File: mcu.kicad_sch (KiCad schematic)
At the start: 9 parts, among them J25 SD_Card_Device, J26 SD_Card_Device

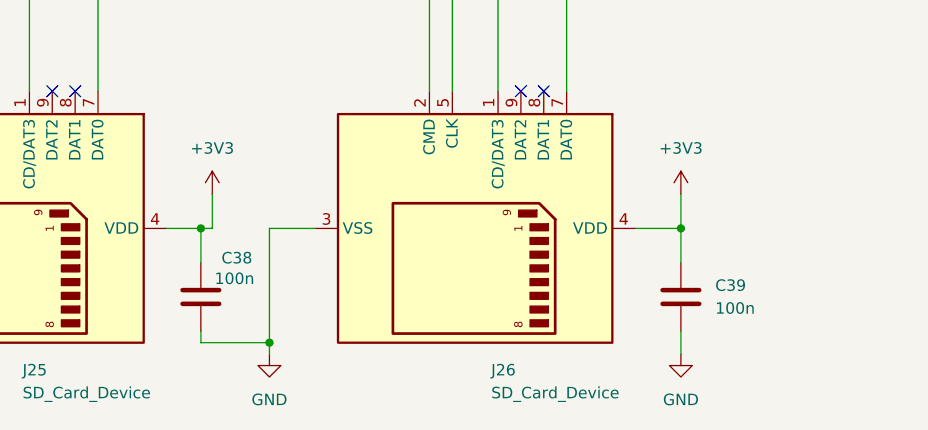
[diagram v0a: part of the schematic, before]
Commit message: Added SD card readers and USB-C for power in.
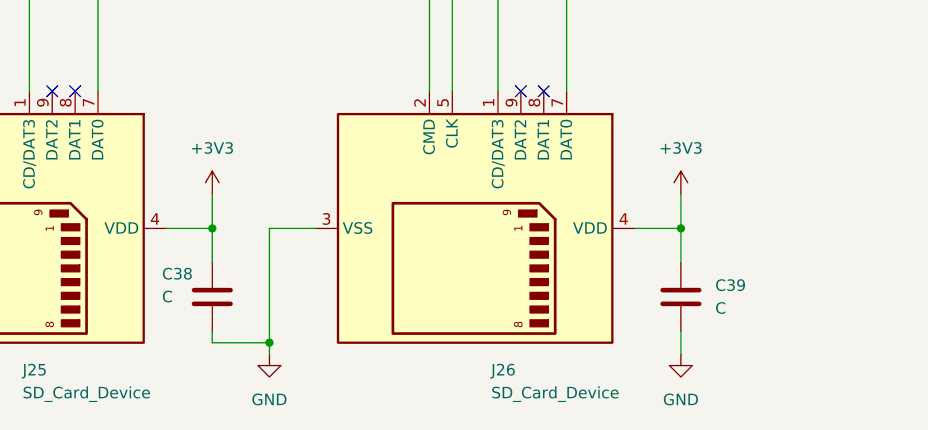
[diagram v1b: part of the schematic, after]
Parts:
- C38, C39: value 100n -> C
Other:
- moved on the sheet: C38
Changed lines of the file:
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@@
-	)
-	(junction
-		(at 72.39 157.48)
-		(diameter 0)
-		(color 0 0 0 0)
 	)
 	(junction
@@
 		(color 0 0 0 0)
 	)
+	(junction
+		(at 73.66 157.48)
+		(diameter 0)
+		(color 0 0 0 0)
+	)
 	(no_connect
 		(at 110.49 142.24)
@@
 	(wire
 		(pts
-			(xy 72.39 170.18) (xy 72.39 168.91)
+			(xy 73.66 170.18) (xy 73.66 168.91)
 		)
 		(stroke
@@
 	(wire
 		(pts
-			(xy 72.39 157.48) (xy 72.39 161.29)
+			(xy 73.66 157.48) (xy 73.66 161.29)
 		)
 		(stroke
@@
 	(wire
 		(pts
-			(xy 72.39 157.48) (xy 73.66 157.48)
-		)
-		(stroke
-			(width 0)
-			(type default)
-		)
-	)
-	(wire
-		(pts
 			(xy 167.64 82.55) (xy 226.06 82.55)
 		)
@@
 	(wire
 		(pts
+			(xy 73.66 157.48) (xy 68.58 157.48)
+		)
+		(stroke
+			(width 0)
+			(type default)
+		)
+	)
+	(wire
+		(pts
 			(xy 128.27 26.67) (xy 123.19 26.67)
 		)
@@
 	(wire
 		(pts
-			(xy 72.39 170.18) (xy 80.01 170.18)
+			(xy 73.66 170.18) (xy 80.01 170.18)
 		)
 		(stroke
@@
 		(pts
 			(xy 45.72 142.24) (xy 45.72 80.01)
-		)
-		(stroke
-			(width 0)
-			(type default)
-		)
-	)
-	(wire
-		(pts
-			(xy 72.39 157.48) (xy 68.58 157.48)
 		)
 		(stroke
@@
 	(symbol
 		(lib_id "Device:C")
-		(at 72.39 165.1 0)
+		(at 73.66 165.1 0)
 		(unit 1)
 		(exclude_from_sim no)
@@
 		(dnp no)
 		(property "Reference" "C38"
-			(at 74.676 160.782 0)
+			(at 68.072 162.56 0)
 			(effects
 				(font
@@
 			)
 		)
-		(property "Value" "100n"
-			(at 73.914 163.068 0)
+		(property "Value" "C"
+			(at 68.072 165.1 0)
 			(effects
 				(font
@@
 		)
 		(property "Footprint" ""
-			(at 73.3552 168.91 0)
+			(at 74.6252 168.91 0)
 			(effects
 				(font
@@
 		)
 		(property "Datasheet" "~"
-			(at 72.39 165.1 0)
+			(at 73.66 165.1 0)
 			(effects
 				(font
@@
 		)
 		(property "Description" "Unpolarized capacitor"
-			(at 72.39 165.1 0)
+			(at 73.66 165.1 0)
 			(effects
 				(font
@@
 			)
 		)
-		(property "Value" "100n"
+		(property "Value" "C"
 			(at 129.54 166.3699 0)
 			(effects

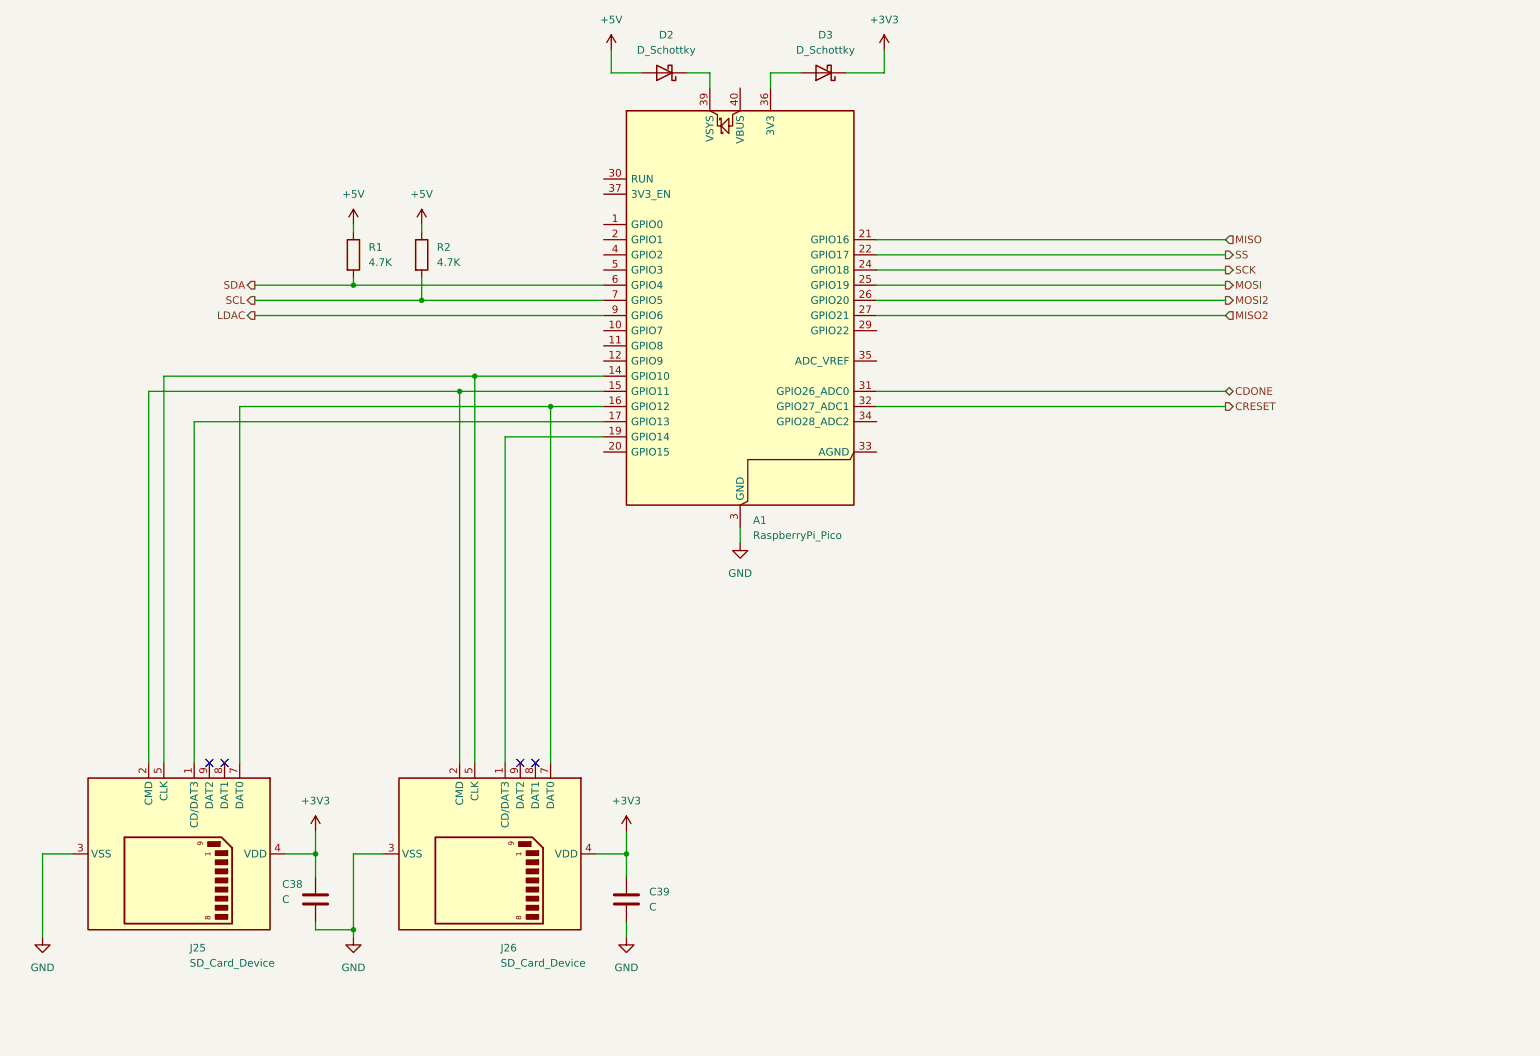
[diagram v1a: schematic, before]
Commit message: reroute dac + comparators
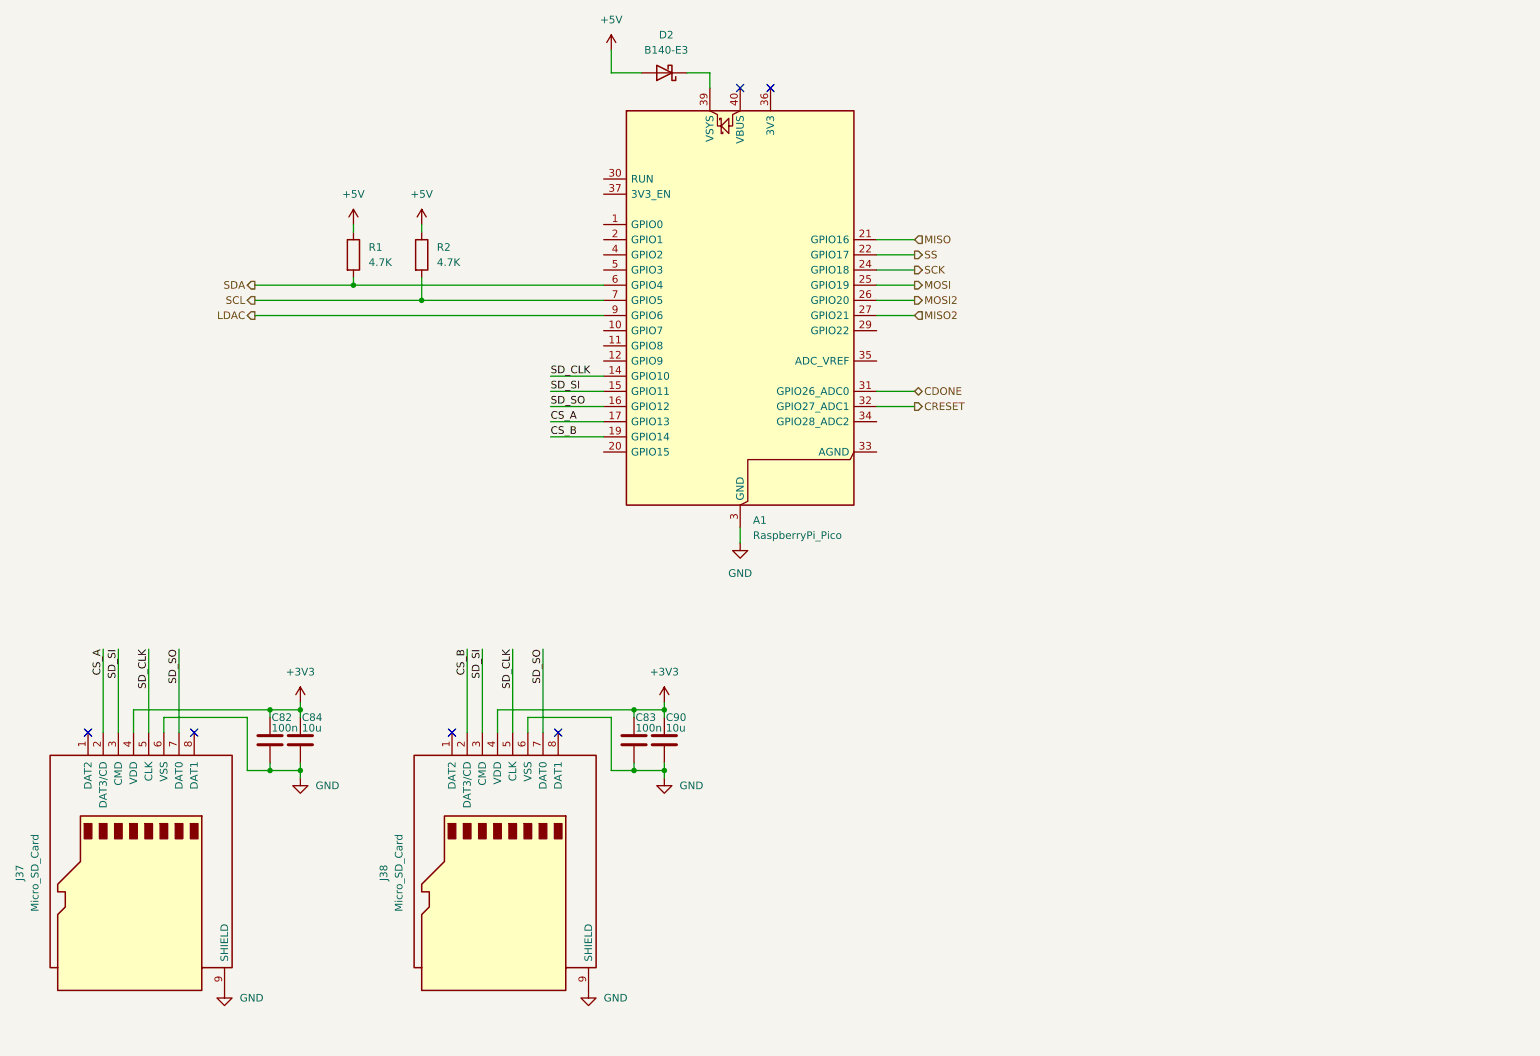
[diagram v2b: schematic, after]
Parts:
- removed C38, C39: C, symbol Device:C
- removed D3: D_Schottky, symbol Device:D_Schottky
- removed J25, J26: SD_Card_Device, symbol Connector:SD_Card_Device
- added C82, C83: 100n, symbol Device:C
- added C84, C90: 10u, symbol Device:C
- added J37, J38: Micro_SD_Card, symbol Connector:Micro_SD_Card
- D2: value D_Schottky -> B140-E3
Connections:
- net +3V3: now also C82.1, C83.1, C84.1, C90.1, J37.4 (VDD), J38.4 (VDD)
- net GND: now also C82.2, C83.2, C84.2, C90.2, J37.6 (VSS), J37.9 (SHIELD), J38.6 (VSS), J38.9 (SHIELD)
- net CS_B: now reaches A1.19 (GPIO14)
- net CS_B: now also J38.2 (DAT3/CD)
- net SD_SI: now reaches A1.15 (GPIO11)
- net SD_SI: now also J37.3 (CMD), J38.3 (CMD)
- net SD_CLK: now reaches A1.14 (GPIO10)
- net SD_CLK: now also J37.5 (CLK), J38.5 (CLK)
- net SD_SO: now reaches A1.16 (GPIO12)
- net SD_SO: now also J37.7 (DAT0), J38.7 (DAT0)
- net CS_A: now reaches A1.17 (GPIO13)
- net CS_A: now also J37.2 (DAT3/CD)
- no-connect marks 4 -> 6

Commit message: rewire
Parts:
- removed A1: RaspberryPi_Pico, Module:RaspberryPi_Pico_Common_Unspecified, symbol MCU_Module:RaspberryPi_Pico
- removed C83: 100n, symbol Device:C
- removed C84, C90: 10u, symbol Device:C
- removed D2: B140-E3, symbol Device:D_Schottky
- added C1, C3: 100n, symbol Device:C
- added C2, C4: 10u, symbol Device:C
- added C30, C31, C33, C35, C36, C5, C6, C7: 100n, Capacitor_SMD:C_0402_1005Metric, symbol Device:C
- added C32, C34: 1u 25V, Capacitor_SMD:C_0402_1005Metric, symbol Device:C
- added C8, C9: 15p, Capacitor_SMD:C_0402_1005Metric, symbol Device:C
- added JP4: ~{RESET}, Jumper:SolderJumper-2_P1.3mm_Open_RoundedPad1.0x1.5mm, symbol Jumper:SolderJumper_2_Open
- added JP5: ~{USB_BOOT}, Jumper:SolderJumper-2_P1.3mm_Open_RoundedPad1.0x1.5mm, symbol Jumper:SolderJumper_2_Open
- added R100, R101: 27R, Resistor_SMD:R_0402_1005Metric, symbol Device:R
- added R112: 10k, Resistor_SMD:R_0402_1005Metric, symbol Device:R
- added R113, R98, R99: 1k, Resistor_SMD:R_0402_1005Metric, symbol Device:R
- added R96, R97: 10k, symbol Device:R
- added U4: W25Q32JVZP, Package_SON:WSON-8-1EP_6x5mm_P1.27mm_EP3.4x4.3mm, symbol Memory_Flash:W25Q32JVZP
- added U5: RP2040, Package_DFN_QFN:QFN-56-1EP_7x7mm_P0.4mm_EP3.2x3.2mm, symbol MCU_RaspberryPi:RP2040
- added Y1: 12 MHz ABM8-272-T3, Crystal:Crystal_SMD_Abracon_ABM8AIG-4Pin_3.2x2.5mm, symbol Device:Crystal_GND24_Small
- C82: footprint (none) -> Capacitor_SMD:C_0402_1005Metric; LCSC (none) -> C307331
- R1, R2: value 4.7K -> 4.7k
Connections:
- net +5V is gone; now on net +3V3: R1.1, R2.1
- net +3V3: now also C33.1, C34.1, C35.1, C36.1, C5.1, C6.1, C7.1, R112.1, R96.1, R97.1, R98.2, U4.8 (VCC), U5.1 (IOVDD), U5.10 (IOVDD), U5.22 (IOVDD), U5.33 (IOVDD), U5.42 (IOVDD), U5.43 (ADC_AVDD), U5.44 (VREG_IN), U5.48 (USB_VDD), U5.49 (IOVDD); no longer J37.4 (VDD), J38.4 (VDD)
- net CS_A: now also U5.11 (GPIO8)
- net CS_B: now also U5.12 (GPIO9)
- net GND: now also C1.2, C2.2, C3.2, C30.2, C31.2, C32.2, C33.2, C34.2, C35.2, C36.2, C4.2, C5.2, C6.2, C7.2, C8.1, C9.1, JP4.1 (A), JP5.1 (A), U4.4 (GND), U4.9 (EP), U5.19 (TESTEN), U5.57 (GND), Y1.2, Y1.4
- net SD_CLK: now also U5.13 (GPIO10)
- net SD_SI: now also U5.14 (GPIO11)
- net SD_SO: now also U5.15 (GPIO12)
- net SCL renamed VREF_SCL
- net VREF_SCL: now also U5.3 (GPIO1)
- net SDA renamed VREF_SDA
- net VREF_SDA: now also U5.2 (GPIO0)
- new net: JP4.2 (B), R98.1, U5.26 (RUN)
- new net: JP5.2 (B), R99.1
- new net: R101.2, U5.46 (USB_DM)
- new net: R100.2, U5.47 (USB_DP)
- new net: C9.2, R113.1, Y1.3
- new net: C3.1, C4.1, J38.4 (VDD)
- new net: C1.1, C2.1, J37.4 (VDD)
- new net +1V1: C30.1, C31.1, C32.1, U5.23 (DVDD), U5.45 (VREG_VOUT), U5.50 (DVDD)
- new net FPGA_CDONE: R97.2, U5.17 (GPIO14)
- new net FPGA_~{CRESET}: R96.2, U5.16 (GPIO13)
- new net QSPI_SCLK: U4.6 (CLK), U5.52 (QSPI_SCLK)
- new net QSPI_SD0: U4.5 (DI/IO_{0}), U5.53 (QSPI_SD0)
- new net QSPI_SD1: U4.2 (DO/IO_{1}), U5.55 (QSPI_SD1)
- new net QSPI_SD2: U4.3 (~{WP}/IO_{2}), U5.54 (QSPI_SD2)
- new net QSPI_SD3: U4.7 (~{HOLD}/~{RESET}/IO_{3}), U5.51 (QSPI_SD3)
- new net QSPI_SS: R112.2, R99.2, U4.1 (~{CS}), U5.56 (QSPI_SS)
- new net SWCLK: U5.24 (SWCLK)
- new net SWD: U5.25 (SWD)
- new net USB_D+: R100.1
- new net USB_D-: R101.1
- new net XIN: C8.2, U5.20 (XIN), Y1.1
- new net XOUT: R113.2, U5.21 (XOUT)
- new net ~{LDAC}0: U5.4 (GPIO2)
- new net ~{LDAC}1: U5.5 (GPIO3)
- new net ~{LDAC}2: U5.6 (GPIO4)
- new net ~{LDAC}3: U5.7 (GPIO5)
- new net ~{LDAC}4: U5.8 (GPIO6)
- new net ~{LDAC}5: U5.9 (GPIO7)
- no-connect marks 6 -> 4
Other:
- note added: "DATA LINK established LED"
- note added: "Next to Pin 44"
- note added: "Next to Pin 45"
- moved on the sheet: J37, J38, R1, R2
